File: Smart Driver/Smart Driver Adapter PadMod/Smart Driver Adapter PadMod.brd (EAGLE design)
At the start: 34.3 x 58.4 mm, 9 parts, among them U2 DRV8353HMRTATWQFN_HMRTAT_TEX-M

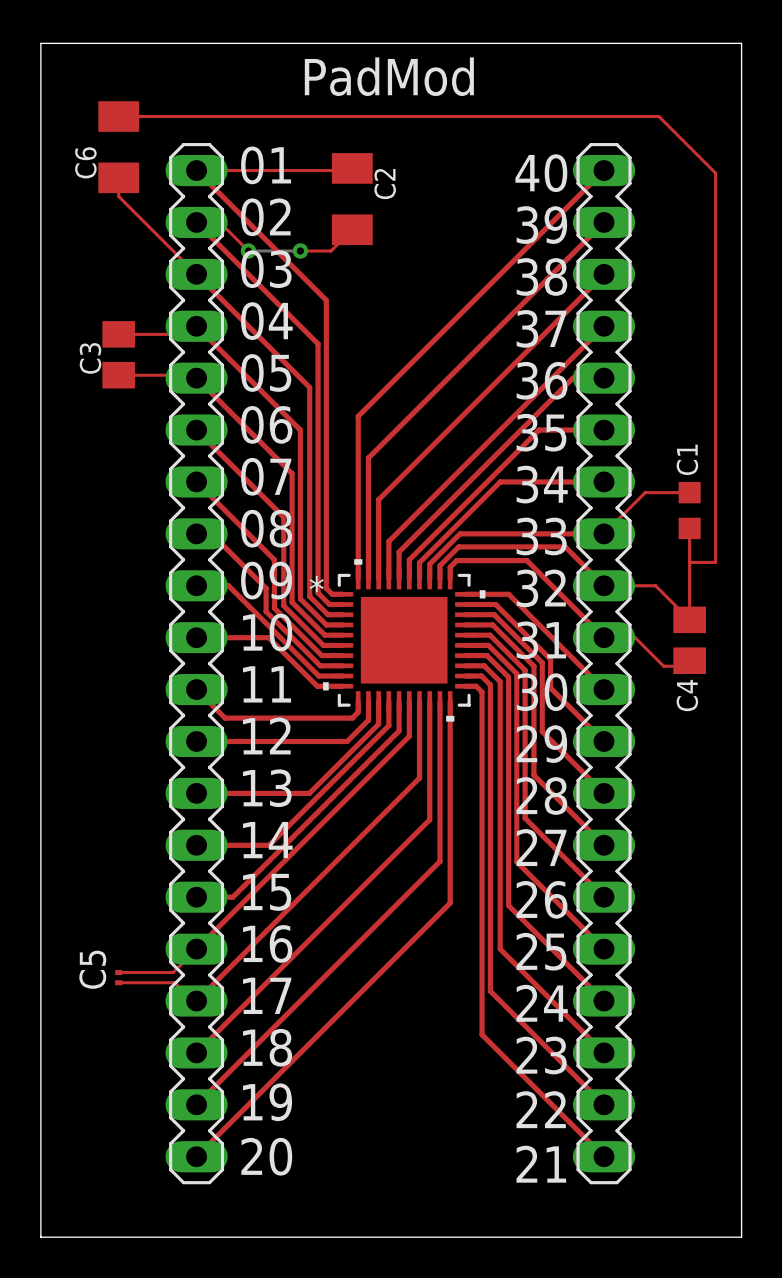
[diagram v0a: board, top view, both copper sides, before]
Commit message: Correcting PadMod Version of PCB
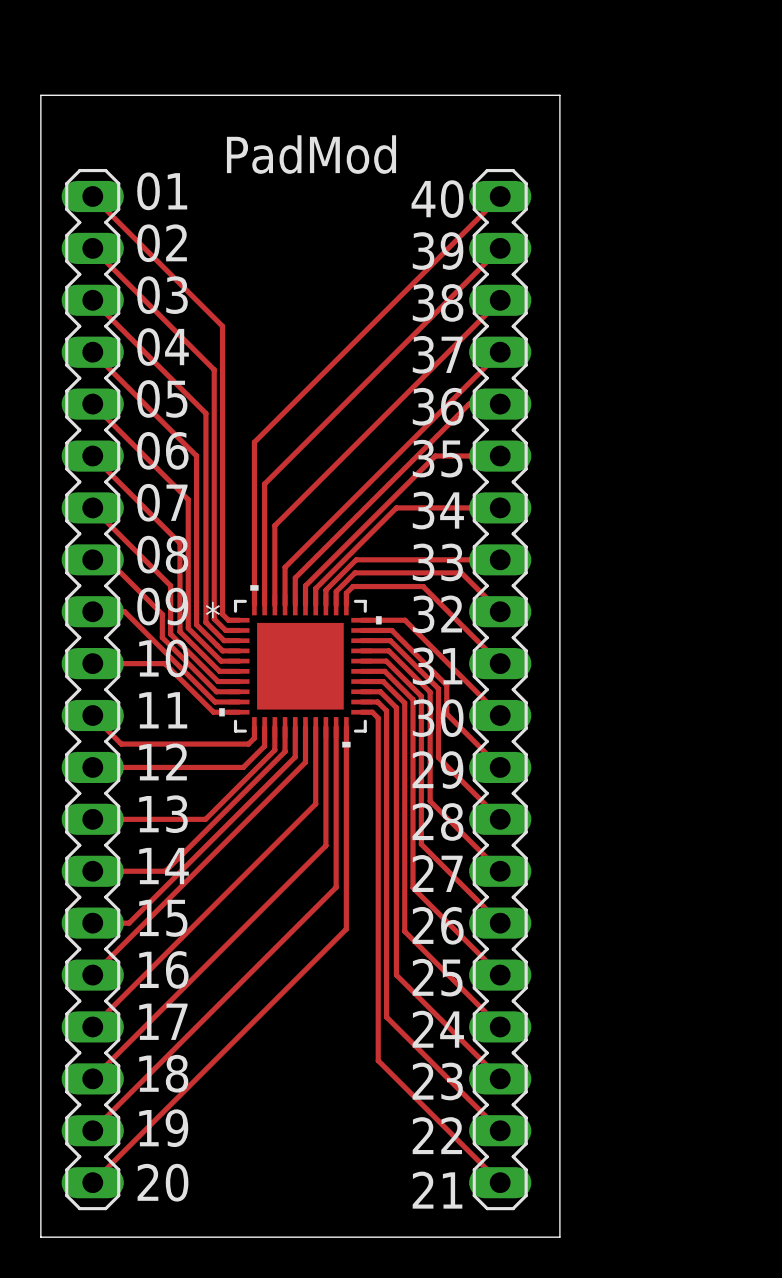
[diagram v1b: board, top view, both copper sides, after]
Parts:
- removed C1: (no value), rcl:C0603K
- removed C2, C6: (no value), rcl:C1206K
- removed C3, C4: (no value), rcl:C0805K
- removed C5: (no value), rcl:C0201
- moved SV2 5.24 mm to (22.5, 26.8)
- moved U2 5.24 mm to (12.7, 27.9)
- moved SV1 5.24 mm to (2.54, 26.8)
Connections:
- removed net N$42: C2.1, SV1.1, U2.1
- new net N$26: SV2.13, U2.33
- net N$1: now also SV1.1, U2.1; no longer C1.1, SV2.13, U2.33
- net N$15: no longer C5.2
- net N$16: no longer C5.1
- net N$27: no longer C1.2, C4.2, C6.2
- net N$28: no longer C4.1
- net N$3: no longer C2.2
- net N$4: no longer C6.1
- net N$5: no longer C3.2
- net N$6: no longer C3.1
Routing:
- net N$27: track 70.1 -> 9.85 mm
- net N$42: track 31.7 -> 0.00 mm
- net N$26: track 0.00 -> 9.87 mm
- net N$1: track 14.9 -> 24.0 mm
- net N$3: track 30.8 -> 22.0 mm, vias 2 -> 0
- net N$4: track 26.5 -> 20.1 mm
- net N$28: track 14.7 -> 9.80 mm
- net N$15: track 20.8 -> 16.4 mm
- net N$16: track 23.4 -> 19.2 mm
- net N$5: track 22.1 -> 18.1 mm
- net N$6: track 19.9 -> 16.1 mm
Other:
- board size 34.3 x 58.4 mm -> 25.4 x 55.9 mm
